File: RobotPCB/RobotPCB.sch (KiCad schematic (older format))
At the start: 40 parts, among them P1 Conn_02x03_Counter_Clockwise, P2 Conn_02x03_Counter_Clockwise, P3 Conn_02x03_Counter_Clockwise, P4 Conn_02x03_Counter_Clockwise, P5 Conn_02x03_Counter_Clockwise, P6 Conn_02x03_Counter_Clockwise, P7 Conn_02x03_Counter_Clockwise, P8 Conn_02x03_Counter_Clockwise, U1 A4988, U2 A4988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

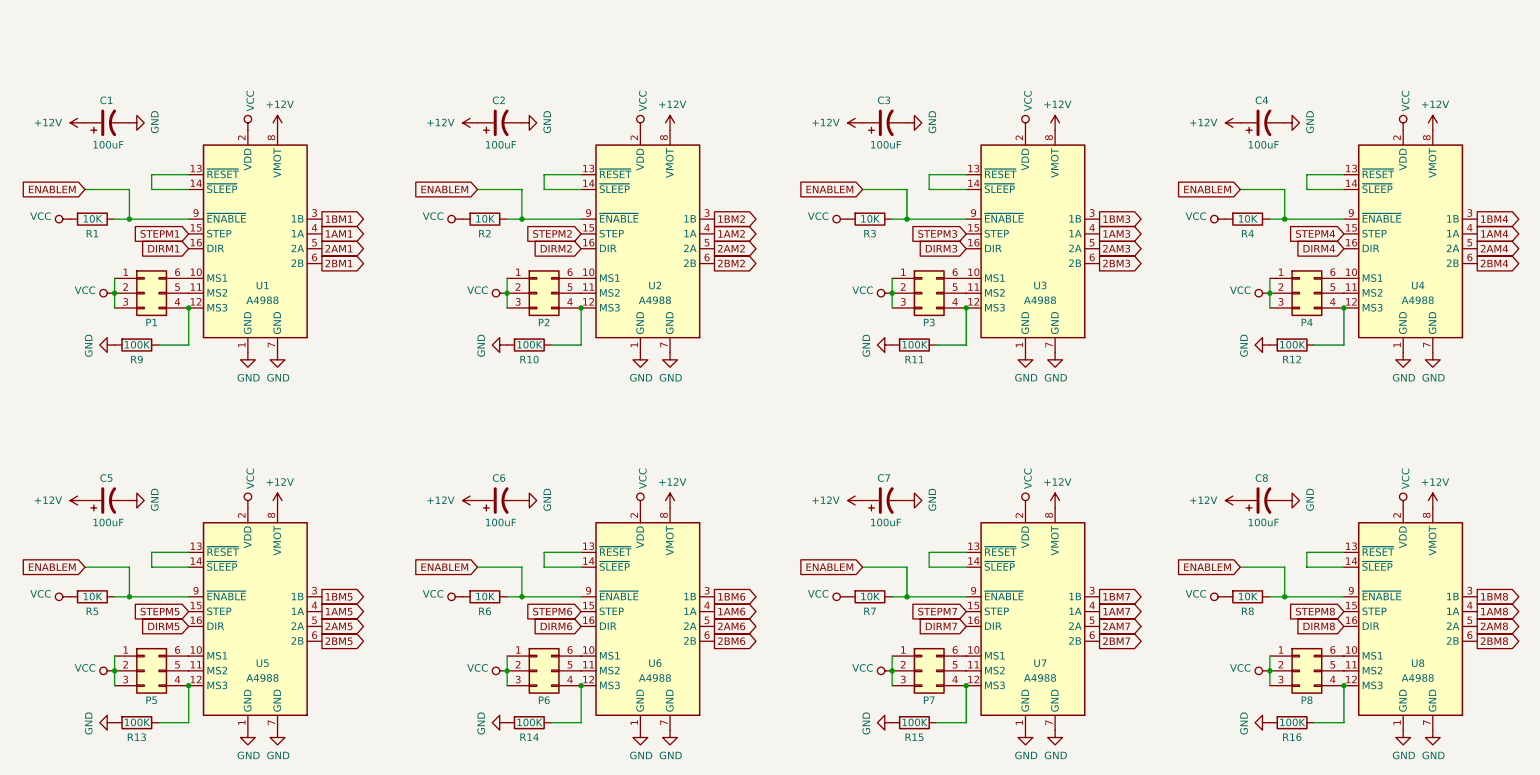
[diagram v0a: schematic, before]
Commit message: Connection & Mega2560 schematic pages added to the KiCad project
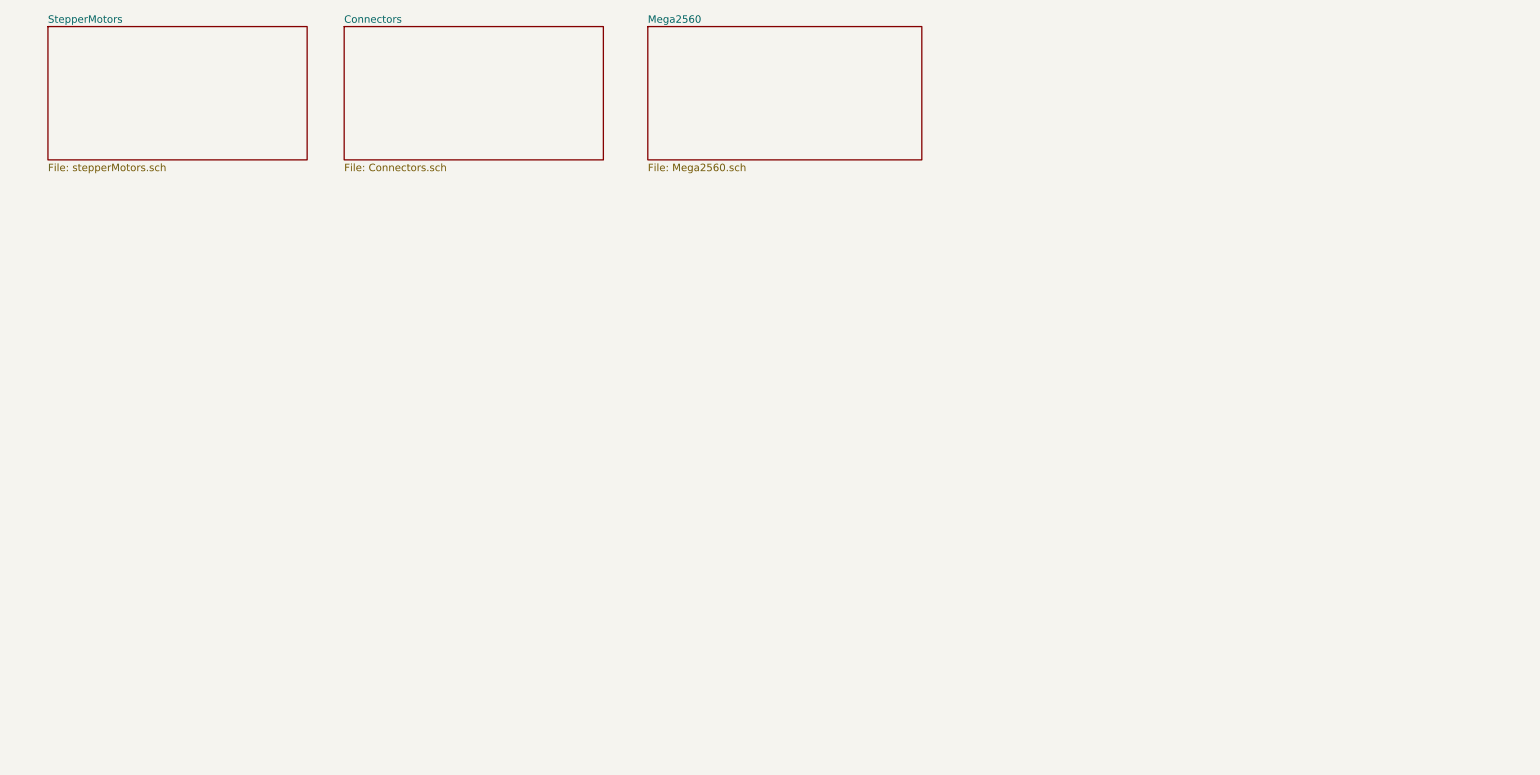
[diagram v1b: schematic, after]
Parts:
- removed C1, C2, C3, C4, C5, C6, C7, C8: 100uF, symbol Device:CP1
- removed P1, P2, P3, P4, P5, P6, P7, P8: Conn_02x03_Counter_Clockwise, symbol Connector_Generic:Conn_02x03_Counter_Clockwise
- removed R1, R2, R3, R4, R5, R6, R7, R8: 10K, symbol Device:R
- removed R10, R11, R12, R13, R14, R15, R16, R9: 100K, symbol Device:R
- removed U1, U2, U3, U4, U5, U6, U7, U8: A4988, Module:Pololu_Breakout-16_15.2x20.3mm, symbol Driver_Motor:Pololu_Breakout_A4988
